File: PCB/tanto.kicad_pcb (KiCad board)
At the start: 4 copper layers, 43 parts, among them J1 USB_C, SW1 SW_Push, U1 STM32F072CBT6, U3 XC6206, U4 USBLC6-2SC6

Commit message: PCB and schematic updates
- added jst-sh connector for UDB compatibility
- removed USB input protection
- routed most traces
- arranged all components
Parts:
- removed F1: 500mA, ScottoKeebs_Components:Fuse_0603
- removed J1: USB_C, ScottoKeebs_Components:USB_C_HRO_TYPE-C-31-M-12
- removed R2, R3: 5.1k, ScottoKeebs_Components:Resistor_0402
- removed REF** (x2): MX_1.00u_PG151101S11, ScottoKeebs_Scotto:MX_Hotswap_1.00u
- removed U4: USBLC6-2SC6, ScottoKeebs_Components:ESD_SOT-23-6
- added J2: SM04B-SRSS-TB, bild:CONN_SM04B-SRSS-TB_JST, B.Cu at (91.5, 88.5)
- moved MX8 263.2 mm to (225.0, 90.3)
- moved MX6 240.6 mm to (179.7, 80.8)
- moved MX7 237.3 mm to (198.8, 80.8)
- moved MX21 236.4 mm to (227.4, 118.9)
- moved MX15 226.6 mm to (203.5, 99.8)
- moved MX5 218.6 mm to (160.7, 80.8)
- moved MX20 211.0 mm to (198.8, 123.6)
- moved MX14 208.3 mm to (184.5, 99.8)
- moved MX4 197.1 mm to (141.6, 80.8)
- moved MX13 191.4 mm to (165.4, 99.8)
- moved MX19 184.9 mm to (167.8, 123.6)
- moved MX12 179.8 mm to (136.9, 99.8)
- moved MX3 176.4 mm to (122.6, 80.8)
- moved MX18 158.5 mm to (134.5, 123.6)
- moved MX11 158.1 mm to (117.8, 99.8)
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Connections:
- U1 pad 26: /B13 -> (no net)
- U1 pad 27: /B14 -> r0c0
- U1 pad 28: /B15 -> r1c0
- U1 pad 29: /A8 -> r1c1
- U1 pad 3: /C14 -> r2c7
- U1 pad 30: /A9 -> r1c2
- U1 pad 31: /A10 -> r1c3
- U1 pad 34: /A13 -> r0c1
- U1 pad 37: /A14 -> r0c2
- U1 pad 38: /A15 -> r0c3
- U1 pad 39: /B3 -> r0c4
- U1 pad 4: /C15 -> r2c5
- U1 pad 40: /B4 -> r0c5
- U1 pad 41: /B5 -> r0c6
- U1 pad 42: /B6 -> r1c4
- U1 pad 43: /B7 -> r1c5
- U1 pad 45: /B8 -> r1c6
- U1 pad 46: /B9 -> r1c7
- U1 pad 5: /F0 -> r2c4
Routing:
- net r0c0: track 0.00 -> 106.0 mm
- net r1c7: track 0.00 -> 84.5 mm
- net r1c0: track 0.00 -> 80.7 mm
- net r2c7: track 0.00 -> 73.7 mm
- net r0c1: track 0.00 -> 70.8 mm
- net r0c6: track 0.00 -> 66.9 mm
- net r1c1: track 0.00 -> 59.4 mm
- net +3.3V: track 71.5 -> 127.8 mm, vias 7 -> 6
- net r0c2: track 0.00 -> 56.1 mm
- net /MCU_D+: track 18.6 -> 73.8 mm
- net /MCU_D-: track 18.6 -> 73.4 mm
- net r1c6: track 0.00 -> 53.8 mm
- net r0c5: track 0.00 -> 47.0 mm
- net r2c5: track 0.00 -> 43.6 mm
- net r1c2: track 0.00 -> 40.4 mm
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- removed copper zone on B.Cu, net /USB_D+
- removed copper zone on F.Cu, net VBUS

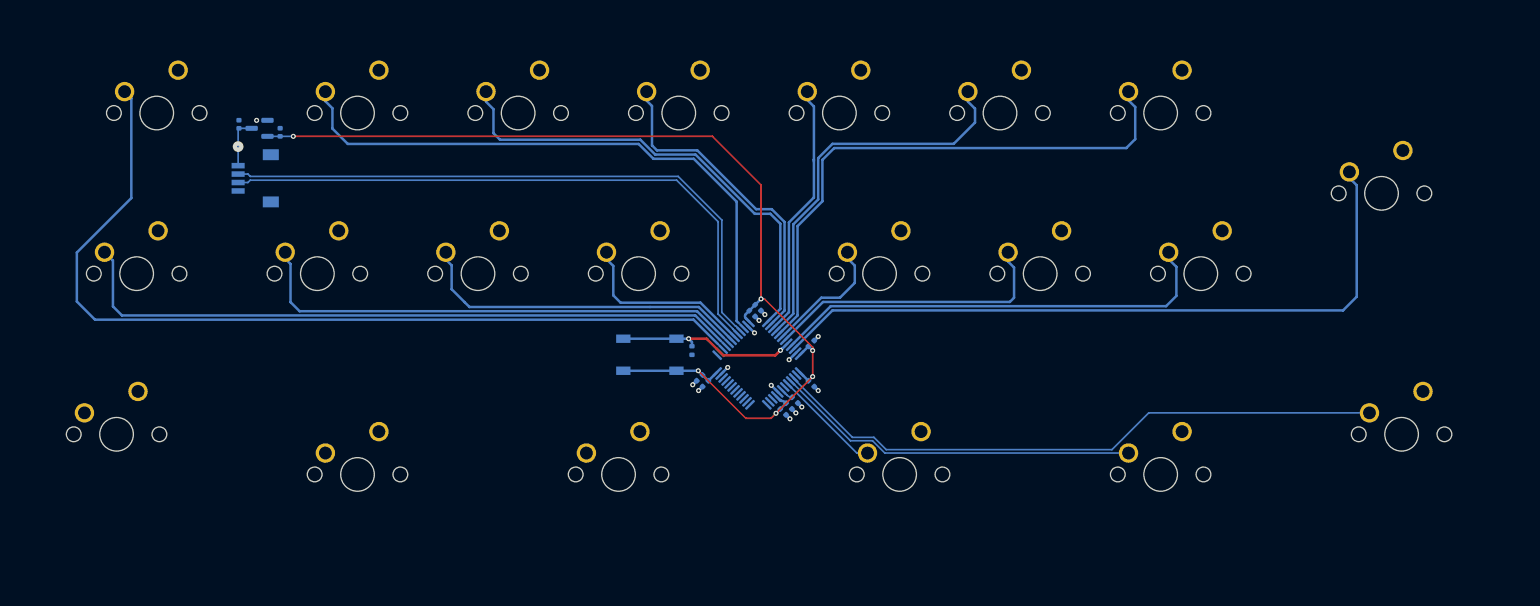
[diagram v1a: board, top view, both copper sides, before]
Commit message: progress on pcb layout
- routed remaining traces
- tidied up routing
-added ground fill
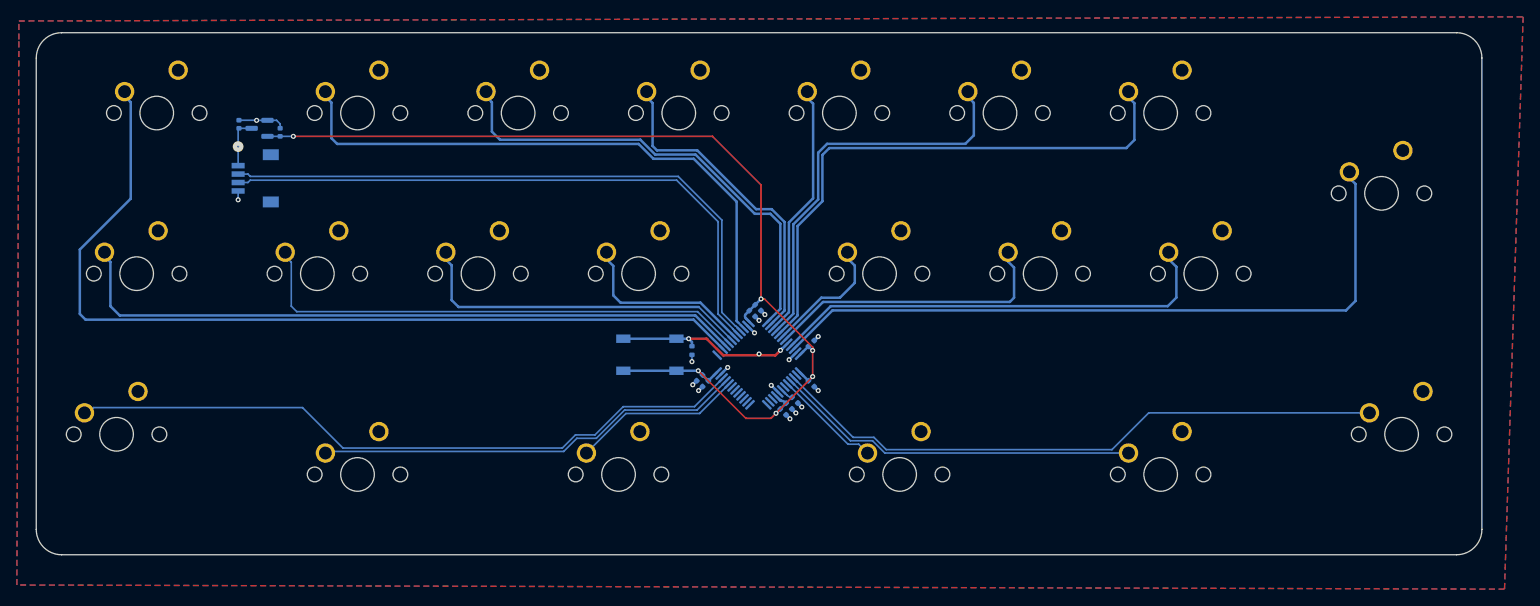
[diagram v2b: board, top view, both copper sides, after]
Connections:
- U1 pad 20: /B2 -> r2c3
- U1 pad 21: /B10 -> r2c2
- U1 pad 22: /B11 -> r2c0
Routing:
- net r2c0: track 0.00 -> 81.4 mm
- net r2c2: track 0.00 -> 51.1 mm
- net r2c3: track 0.00 -> 20.3 mm
- net GND: track 11.2 -> 18.6 mm, vias 14 -> 16
- net r1c0: track 80.7 -> 82.7 mm
- net r0c0: track 106.0 -> 107.2 mm
- net r1c1: track 59.4 -> 60.4 mm
- net r0c5: track 47.0 -> 48.1 mm
- net r1c2: track 40.4 -> 41.2 mm
- net r0c1: track 70.8 -> 71.5 mm
- net /BOOT0: vias 2 -> 3
- added copper zone on B.Cu, net GND
- added copper zone on F.Cu, net GND
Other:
- board outline added: 171.5 x 61.9 mm

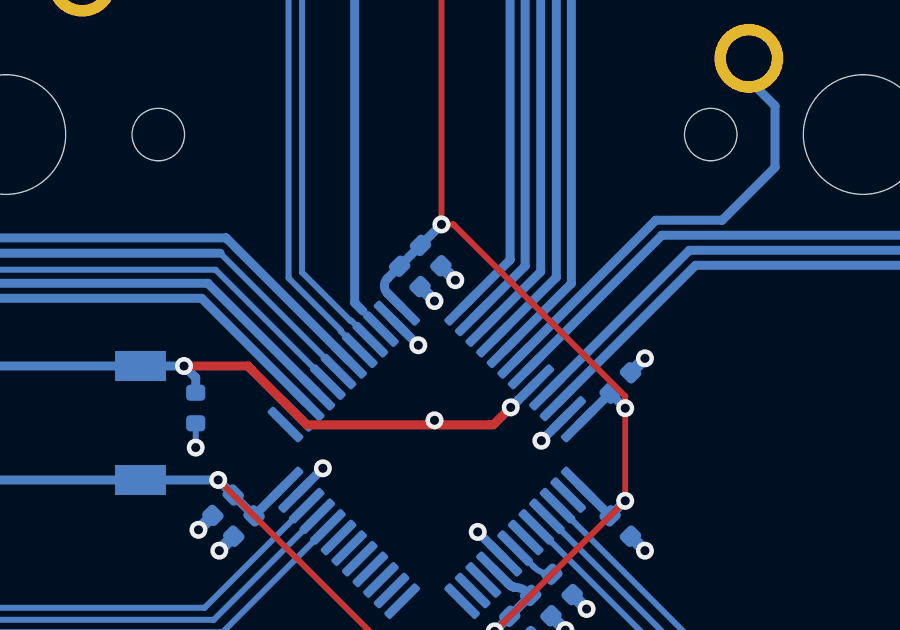
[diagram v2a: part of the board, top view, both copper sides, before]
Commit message: fixed DRC errors
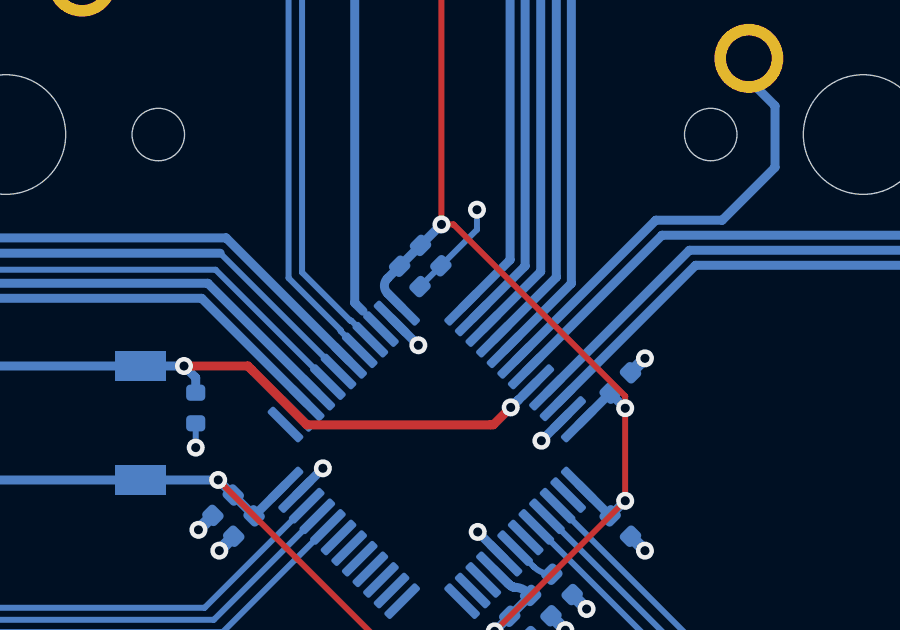
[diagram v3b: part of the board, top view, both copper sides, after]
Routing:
- net GND: track 18.6 -> 20.6 mm, vias 16 -> 15
- net /BOOT0: vias 3 -> 2
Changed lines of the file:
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@@
-	)
-	(via
-		(at 151.854965 104.661256)
-		(size 0.6)
-		(drill 0.3)
-		(layers "F.Cu" "B.Cu")
-		(net 1)
 	)
 	(via
@@
 	)
 	(via
-		(at 151.160231 105.355988)
-		(size 0.6)
-		(drill 0.3)
-		(layers "F.Cu" "B.Cu")
+		(at 152.577446 102.311904)
+		(size 0.6)
+		(drill 0.3)
+		(layers "F.Cu" "B.Cu")
+		(free yes)
 		(net 1)
 	)
@@
 	)
 	(segment
-		(start 150.679399 104.875151)
-		(end 151.160231 105.355983)
-		(width 0.4)
-		(layer "B.Cu")
-		(net 1)
-	)
-	(segment
 		(start 93.942446 81.621904)
 		(end 94.362446 82.041904)
@@
 	)
 	(segment
-		(start 151.160231 105.355983)
-		(end 151.160231 105.355988)
-		(width 0.4)
-		(layer "B.Cu")
-		(net 1)
-	)
-	(segment
 		(start 146.548124 111.824246)
 		(end 147.440846 110.931524)
@@
 	)
 	(segment
+		(start 152.577446 102.977108)
+		(end 152.577446 102.311904)
+		(width 0.2)
+		(layer "B.Cu")
+		(net 1)
+	)
+	(segment
 		(start 157.695664 113.19603)
 		(end 158.176497 113.676864)
@@
 	)
 	(segment
+		(start 151.37413 104.180424)
+		(end 152.577446 102.977108)
+		(width 0.2)
+		(layer "B.Cu")
+		(net 1)
+	)
+	(segment
 		(start 157.695662 107.747776)
 		(end 158.176495 107.266943)
@@
 	)
 	(segment
-		(start 151.854963 104.661256)
-		(end 151.854965 104.661256)
-		(width 0.4)
+		(start 150.679404 104.87515)
+		(end 151.37413 104.180424)
+		(width 0.2)
 		(layer "B.Cu")
 		(net 1)
@@
 	)
 	(segment
-		(start 151.374128 104.18042)
-		(end 151.854963 104.661256)
-		(width 0.4)
+		(start 150.679401 104.87515)
+		(end 150.679404 104.87515)
+		(width 0.2)
 		(layer "B.Cu")
 		(net 1)
@@
 		(size 0.6)
 		(drill 0.3)
-		(layers "F.Cu" "B.Cu")
-		(net 15)
-	)
-	(via
-		(at 151.162446 109.331904)
-		(size 0.6)
-		(drill 0.3)

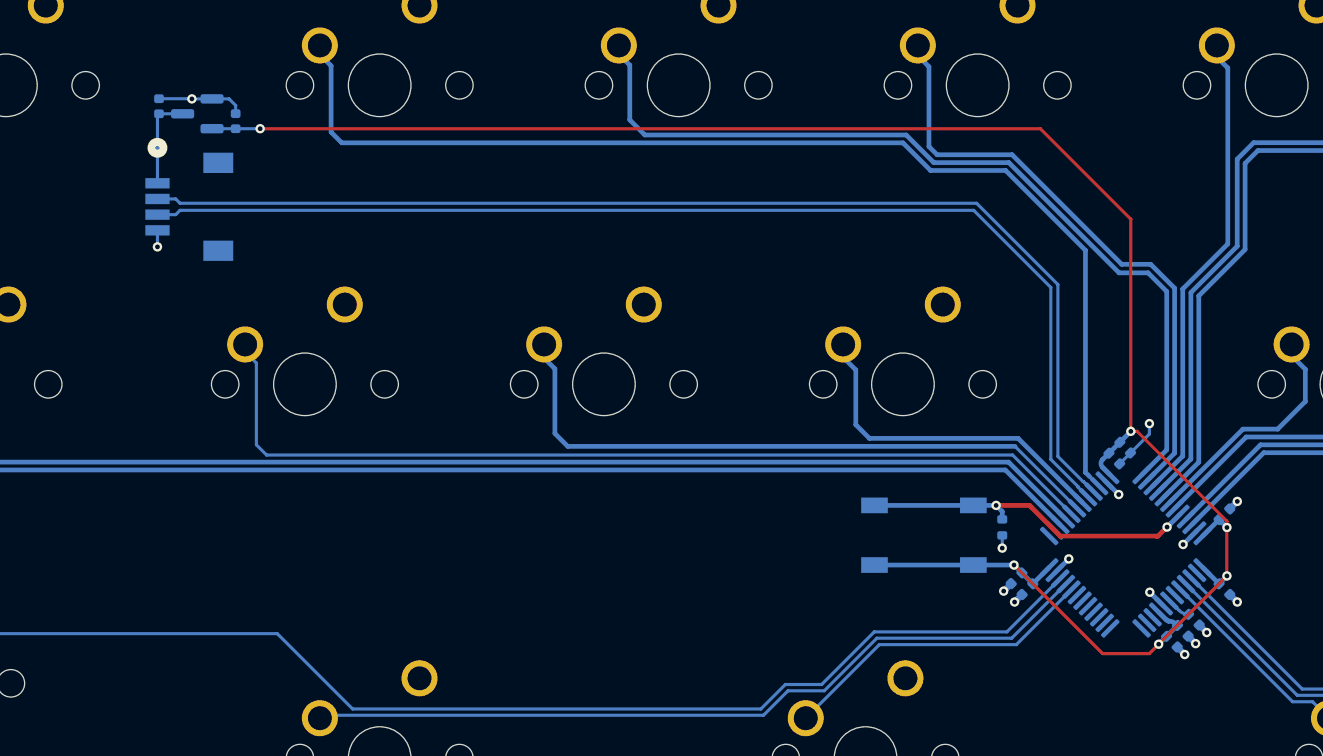
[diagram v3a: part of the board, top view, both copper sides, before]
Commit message: minimized front copper layer signal routing
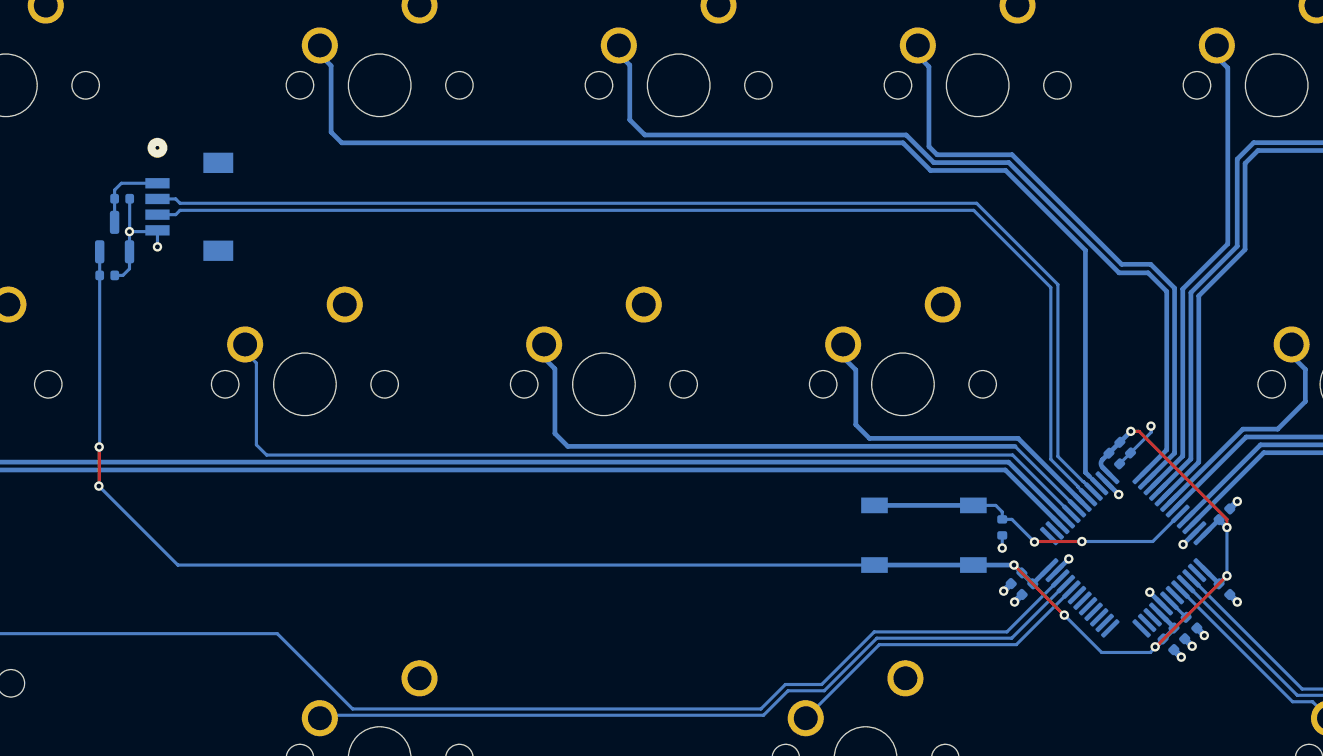
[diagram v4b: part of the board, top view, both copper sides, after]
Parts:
- moved C9 12.8 mm to (86.2, 92.9), turned to 0 degrees
- moved U3 9.46 mm to (86.6, 90.4), turned to 90 degrees
- moved C8 6.34 mm to (87.1, 88.0), turned to 0 degrees
- moved C14 0.28 mm to (154.5, 115.7)
- moved C15 0.28 mm to (153.8, 116.4)
- moved C7 0.25 mm to (155.3, 115.0)
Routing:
- net +3.3V: track 127.8 -> 119.5 mm, vias 6 -> 8
- net GND: track 20.6 -> 22.4 mm
- net +5V: track 5.97 -> 5.11 mm
- net /BOOT0: track 22.3 -> 21.5 mm

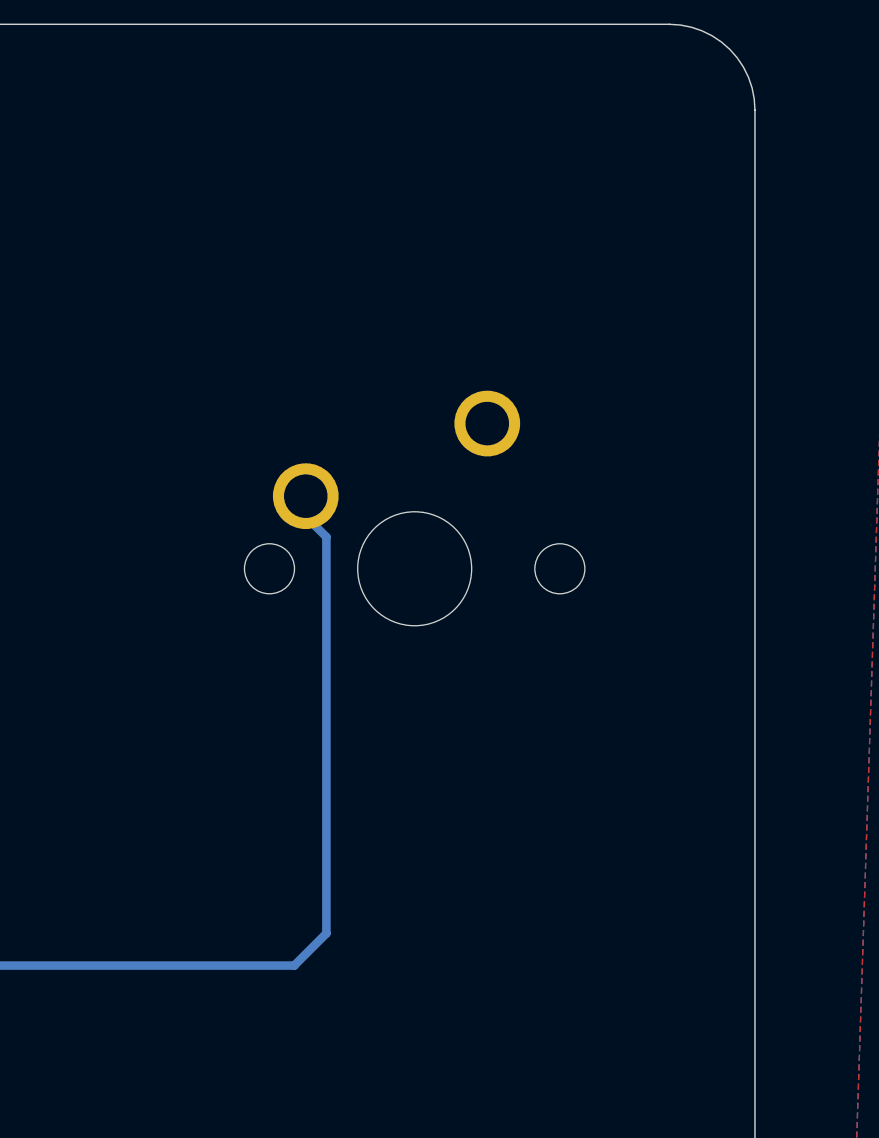
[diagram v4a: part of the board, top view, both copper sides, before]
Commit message: added ISO enter stab footprint
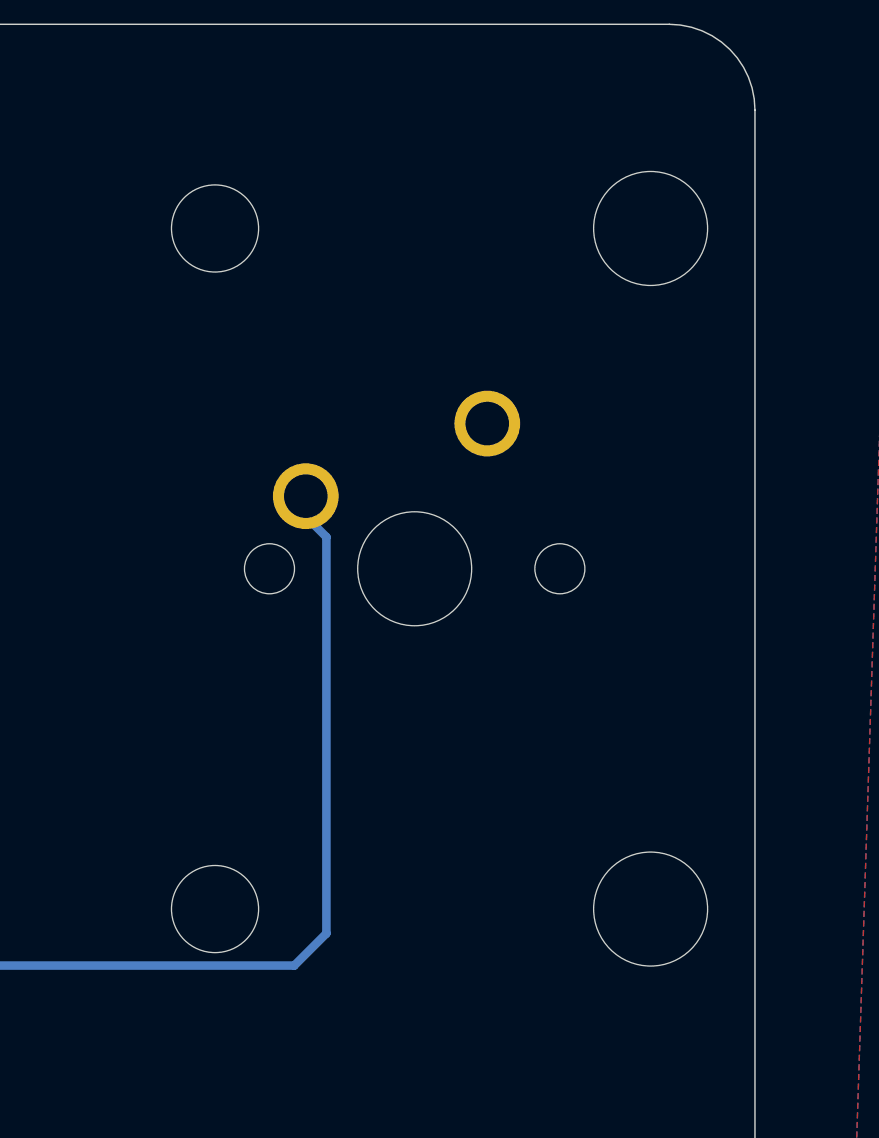
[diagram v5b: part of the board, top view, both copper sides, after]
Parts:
- added REF**: STAB_MX_ISO, PCM_marbastlib-mx:STAB_MX_ISO, F.Cu at (225.0, 90.3)
